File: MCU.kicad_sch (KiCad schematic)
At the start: 30 parts, among them J301 TC-2030-NL, SW301 SW_MEC_5G, SW302 SW_MEC_5G, SW303 SW_MEC_5G, SW304 SW_MEC_5G, U301 STM32G030C8T6, Y301 16MHz

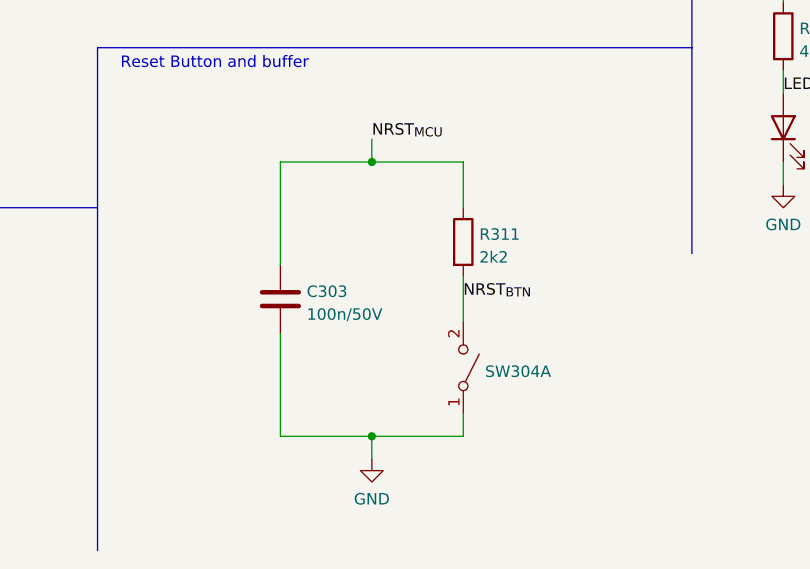
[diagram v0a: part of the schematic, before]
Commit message: Added Testpoints
Schematic and PCB updated
Also probably some other smaller changes that I forgot about
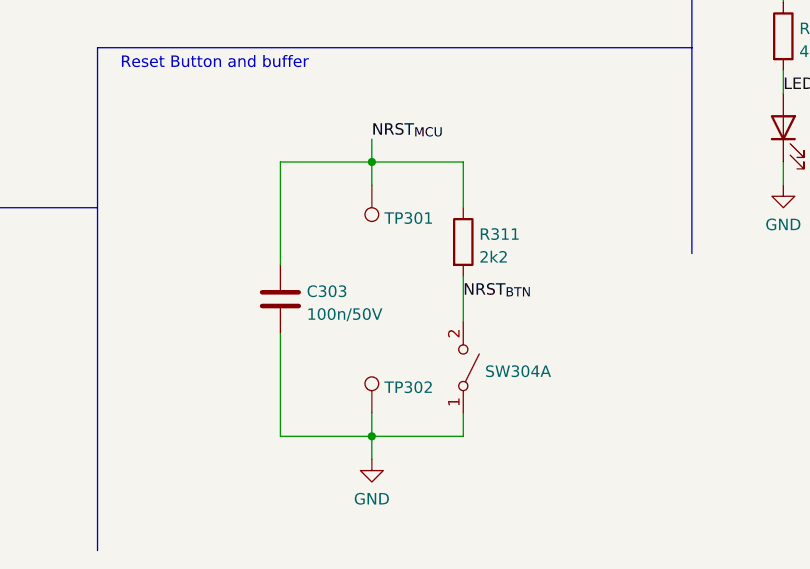
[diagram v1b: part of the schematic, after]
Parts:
- added TP301, TP302: TestPoint, TestPoint:TestPoint_Loop_D1.80mm_Drill1.0mm_Beaded, symbol Connector:TestPoint
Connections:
- net GND: now also TP302.1
- net NRST_{MCU}: now also TP301.1
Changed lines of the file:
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@@
+    (stroke (width 0) (type default) (color 0 0 0 0))
+  )
+  (wire (pts (xy 142.24 182.88) (xy 142.24 185.42))
     (stroke (width 0) (type default) (color 0 0 0 0))
   )
@@
   )
   (wire (pts (xy 266.7 30.48) (xy 266.7 35.56))
+    (stroke (width 0) (type default) (color 0 0 0 0))
+  )
+  (wire (pts (xy 142.24 157.48) (xy 142.24 154.94))
     (stroke (width 0) (type default) (color 0 0 0 0))
   )
@@
     (pin "2")
   )
+  (symbol (lib_id "Connector:TestPoint") (at 142.24 182.88 0) (unit 1)
+    (in_bom yes) (on_board yes) (fields_autoplaced)
+    (property "Reference" "TP302" (id 0) (at 143.637 180.0118 0)
+      (effects (font (size 1.27 1.27)) (justify left))
+    )
+    (property "Value" "TestPoint" (id 1) (at 143.637 181.2802 0)
+      (effects (font (size 1.27 1.27)) (justify left) hide)
+    )
+    (property "Footprint" "TestPoint:TestPoint_Loop_D1.80mm_Drill1.0mm_Beaded" (id 2) (at 147.32 182.88 0)
+      (effects (font (size 1.27 1.27)) hide)
+    )
+    (property "Datasheet" "~" (id 3) (at 147.32 182.88 0)
+      (effects (font (size 1.27 1.27)) hide)
+    )
+    (property "LCSC" "C238122" (id 4) (at 142.24 182.88 0)
+      (effects (font (size 1.27 1.27)) hide)
+    )
+    (pin "1")
+  )
   (symbol (lib_id "power:+3.3V") (at 33.02 167.64 0) (unit 1)
     (in_bom yes) (on_board yes) (fields_autoplaced)
@@
       (effects (font (size 1.27 1.27)) hide)
     )
+    (pin "1")
+  )
+  (symbol (lib_id "Connector:TestPoint") (at 142.24 157.48 180) (unit 1)
+    (in_bom yes) (on_board yes) (fields_autoplaced)
+    (property "Reference" "TP301" (id 0) (at 143.637 161.2158 0)
+      (effects (font (size 1.27 1.27)) (justify right))
+    )
+    (property "Value" "TestPoint" (id 1) (at 140.843 159.0798 0)
+      (effects (font (size 1.27 1.27)) (justify left) hide)
+    )
+    (property "Footprint" "TestPoint:TestPoint_Loop_D1.80mm_Drill1.0mm_Beaded" (id 2) (at 137.16 157.48 0)
+      (effects (font (size 1.27 1.27)) hide)
+    )
+    (property "Datasheet" "~" (id 3) (at 137.16 157.48 0)
+      (effects (font (size 1.27 1.27)) hide)
+    )
+    (property "LCSC" "C238122" (id 4) (at 142.24 157.48 0)
+      (effects (font (size 1.27 1.27)) hide)
+    )

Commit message: Fix DRCs and BOM errors
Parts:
- C306: LCSC (none) -> C15849
- SW301, SW302, SW303, SW304: LCSC (none) -> C318884
- U301: LCSC (none) -> C529329
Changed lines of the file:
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@@
+      (effects (font (size 1.27 1.27)) hide)
+    )
+    (property "LCSC" "C318884" (id 4) (at 200.66 91.44 0)
       (effects (font (size 1.27 1.27)) hide)
     )
@@
     )
     (property "Datasheet" "~" (id 3) (at 187.96 91.44 0)
+      (effects (font (size 1.27 1.27)) hide)
+    )
+    (property "LCSC" "C318884" (id 4) (at 187.96 91.44 0)
       (effects (font (size 1.27 1.27)) hide)
     )
@@
       (effects (font (size 1.27 1.27)) hide)
     )
+    (property "LCSC" "C318884" (id 4) (at 213.36 91.44 0)
+      (effects (font (size 1.27 1.27)) hide)
+    )
     (pin "1")
     (pin "2")
@@
       (effects (font (size 1.27 1.27)) hide)
     )
+    (property "LCSC" "C15849" (id 4) (at 73.66 176.53 0)
+      (effects (font (size 1.27 1.27)) hide)
+    )
     (pin "1")
     (pin "2")
@@
     (property "Datasheet" "STM32G030C8T6" (id 3) (at 55.88 43.18 0)
       (effects (font (size 1.27 1.27) italic) hide)
+    )
+    (property "LCSC" "C529329" (id 4) (at 55.88 43.18 0)
+      (effects (font (size 1.27 1.27)) hide)
     )
     (pin "1")
@@
       (effects (font (size 1.27 1.27)) hide)
     )
+    (property "LCSC" "C318884" (id 4) (at 152.4 177.8 0)
+      (effects (font (size 1.27 1.27)) hide)
+    )
